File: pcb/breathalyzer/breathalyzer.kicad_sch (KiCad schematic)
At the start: 26 parts, among them IC1 TPS3840DL25DBVR, IC2 HEF4543BT,653, J1 Conn_01x07_Pin, SW1 PTS636SK43SMTR, SW2 430162085826, U1 STM32F030K6Tx, U2 TLV73325PDBV, U3 TLV61070ADBV, U4 HDSP-211C, U5 HDSP-211C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

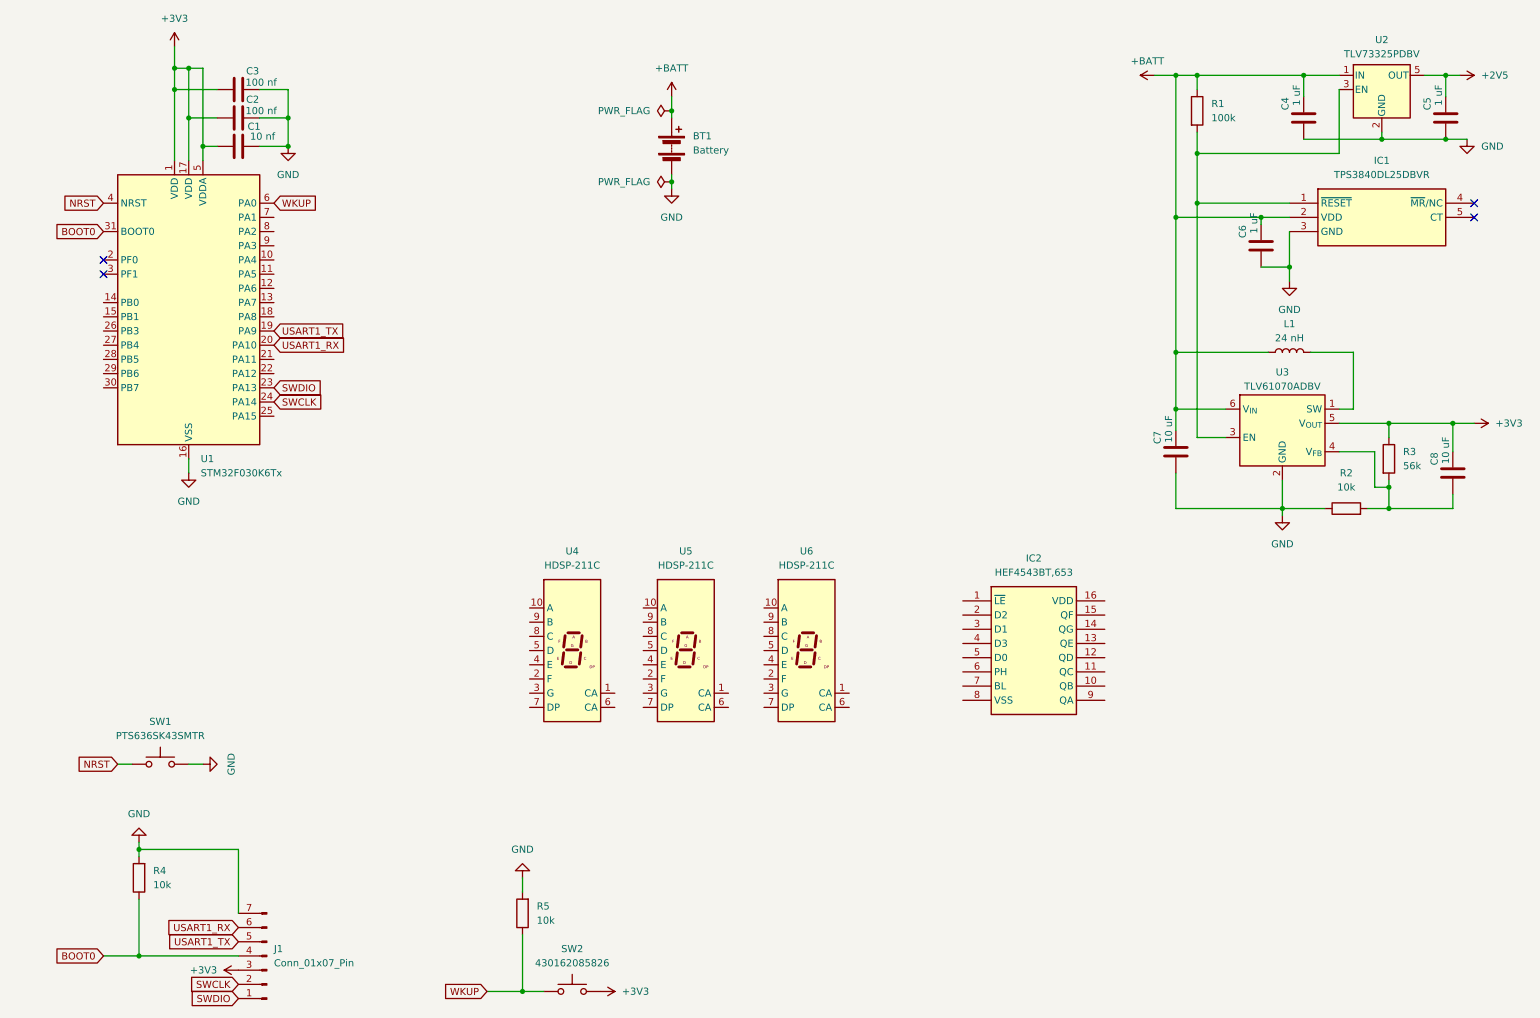
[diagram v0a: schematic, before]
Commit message: numeric LCD display and driver
+5V boost
previous parts scrapped
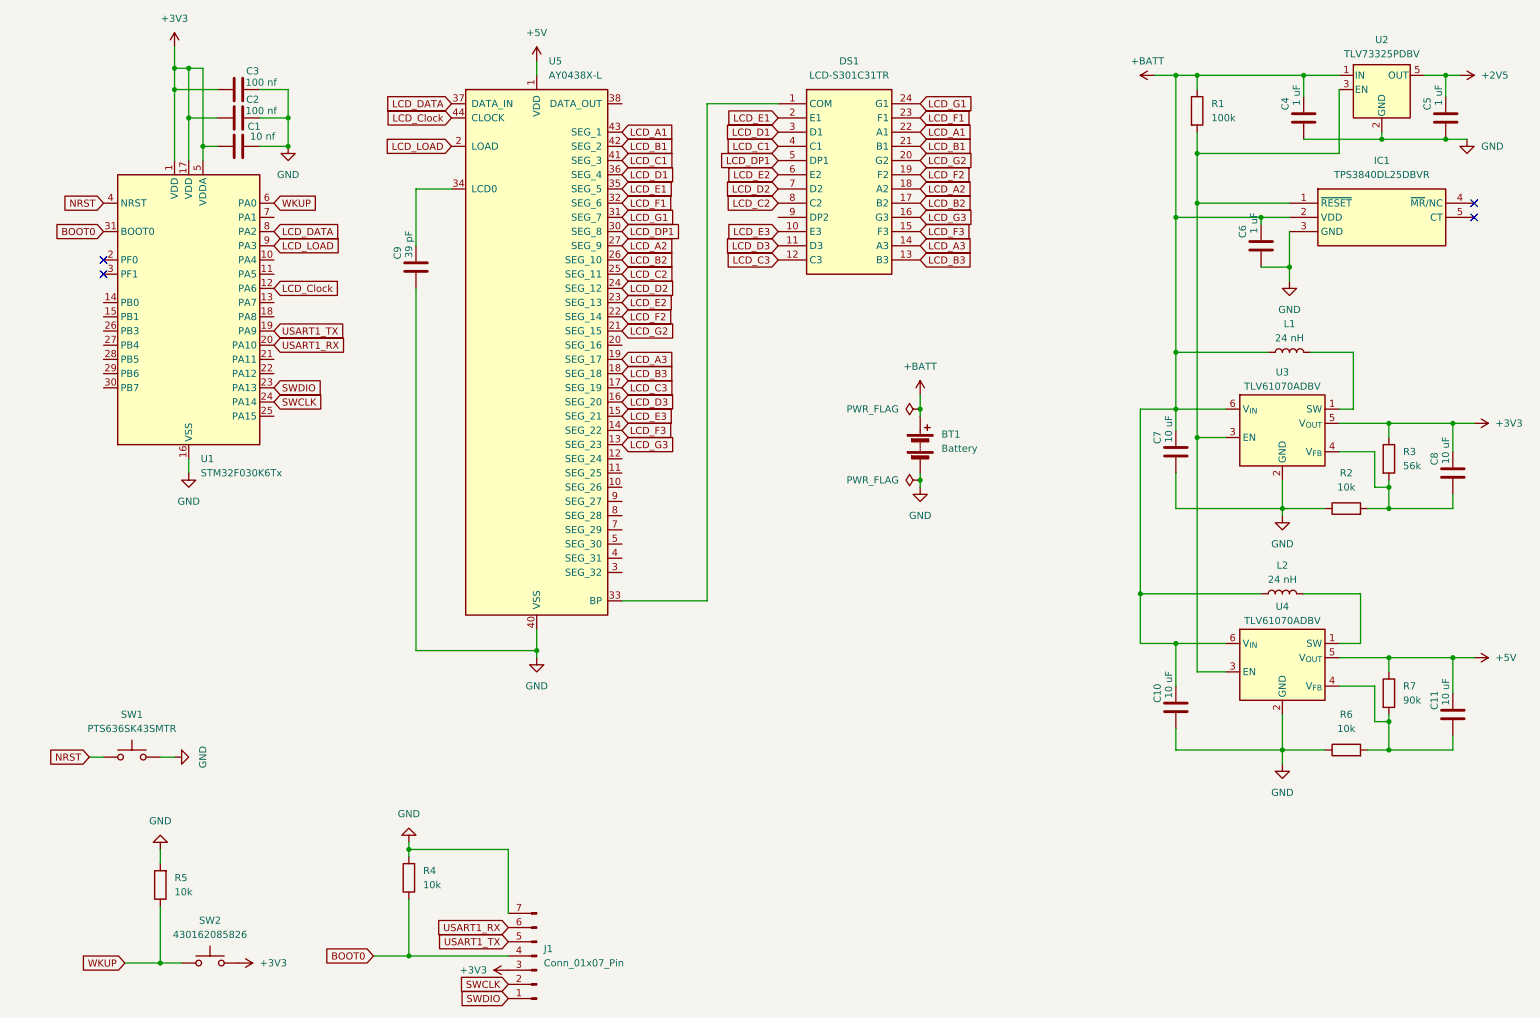
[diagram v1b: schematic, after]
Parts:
- removed IC2: HEF4543BT,653, breathalyzer:HEF4543BT653, symbol breathalyzer:HEF4543BT,653
- removed U4, U5, U6: HDSP-211C, breathalyzer:LDSA3502RDSUG, symbol Display_Character:HDSP-7401
- added C10, C11: 10 uF, Capacitor_SMD:C_0805_2012Metric, symbol Device:C
- added C9: 39 pF, Capacitor_SMD:C_0603_1608Metric, symbol Device:C
- added DS1: LCD-S301C31TR, LCD-S301C31TR, symbol breathalyzer:LCD-S301C31TR
- added L2: 24 nH, Inductor_SMD:L_1008_2520Metric, symbol Device:L
- added R6: 10k, Resistor_SMD:R_0603_1608Metric, symbol Device:R
- added R7: 90k, Resistor_SMD:R_1206_3216Metric, symbol Device:R
- added U4: TLV61070ADBV, Package_TO_SOT_SMD:SOT-23-6, symbol Regulator_Switching:TLV61070ADBV
- added U5: AY0438X-L, Package_LCC:PLCC-44, symbol Driver_Display:AY0438X-L
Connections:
- net +BATT: now also C10.2, L2.1, U4.6 (V_{IN})
- net GND: now also C10.1, C9.1, R6.1, U4.2 (GND), U5.40 (VSS)
- net at IC1.1 (~{RESET}), R1.2, U2.3 (EN)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: now also U4.3 (EN)
- net LCD_Clock: now reaches U1.12 (PA6)
- net LCD_Clock: now also U5.44 (CLOCK)
- net LCD_DATA: now reaches U1.8 (PA2)
- net LCD_DATA: now also U5.37 (DATA_IN)
- net LCD_LOAD: now reaches U1.9 (PA3)
- net LCD_LOAD: now also U5.2 (LOAD)
- new net: C11.1, R6.2, R7.2, U4.4 (V_{FB})
- new net: L2.2, U4.1 (SW)
- new net: C9.2, U5.34 (LCD0)
- new net: DS1.1 (COM), U5.33 (BP)
- new net +5V: C11.2, R7.1, U4.5 (V_{OUT}), U5.1 (VDD)
- new net LCD_A1: DS1.22 (A1), U5.43 (SEG_1)
- new net LCD_A2: DS1.18 (A2), U5.27 (SEG_9)
- new net LCD_A3: DS1.14 (A3), U5.19 (SEG_17)
- new net LCD_B1: DS1.21 (B1), U5.42 (SEG_2)
- new net LCD_B2: DS1.17 (B2), U5.26 (SEG_10)
- new net LCD_B3: DS1.13 (B3), U5.18 (SEG_18)
- new net LCD_C1: DS1.4 (C1), U5.41 (SEG_3)
- new net LCD_C2: DS1.8 (C2), U5.25 (SEG_11)
- new net LCD_C3: DS1.12 (C3), U5.17 (SEG_19)
- new net LCD_D1: DS1.3 (D1), U5.36 (SEG_4)
- new net LCD_D2: DS1.7 (D2), U5.24 (SEG_12)
- new net LCD_D3: DS1.11 (D3), U5.16 (SEG_20)
- new net LCD_DP1: DS1.5 (DP1), U5.30 (SEG_8)
- new net LCD_E1: DS1.2 (E1), U5.35 (SEG_5)
- new net LCD_E2: DS1.6 (E2), U5.23 (SEG_13)
- new net LCD_E3: DS1.10 (E3), U5.15 (SEG_21)
- new net LCD_F1: DS1.23 (F1), U5.32 (SEG_6)
- new net LCD_F2: DS1.19 (F2), U5.22 (SEG_14)
- new net LCD_F3: DS1.15 (F3), U5.14 (SEG_22)
- new net LCD_G1: DS1.24 (G1), U5.31 (SEG_7)
- new net LCD_G2: DS1.20 (G2), U5.21 (SEG_15)
- new net LCD_G3: DS1.16 (G3), U5.13 (SEG_23)
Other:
- moved on the sheet: BT1, J1, R4, R5, SW1, SW2

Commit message: removed 3V3 boost
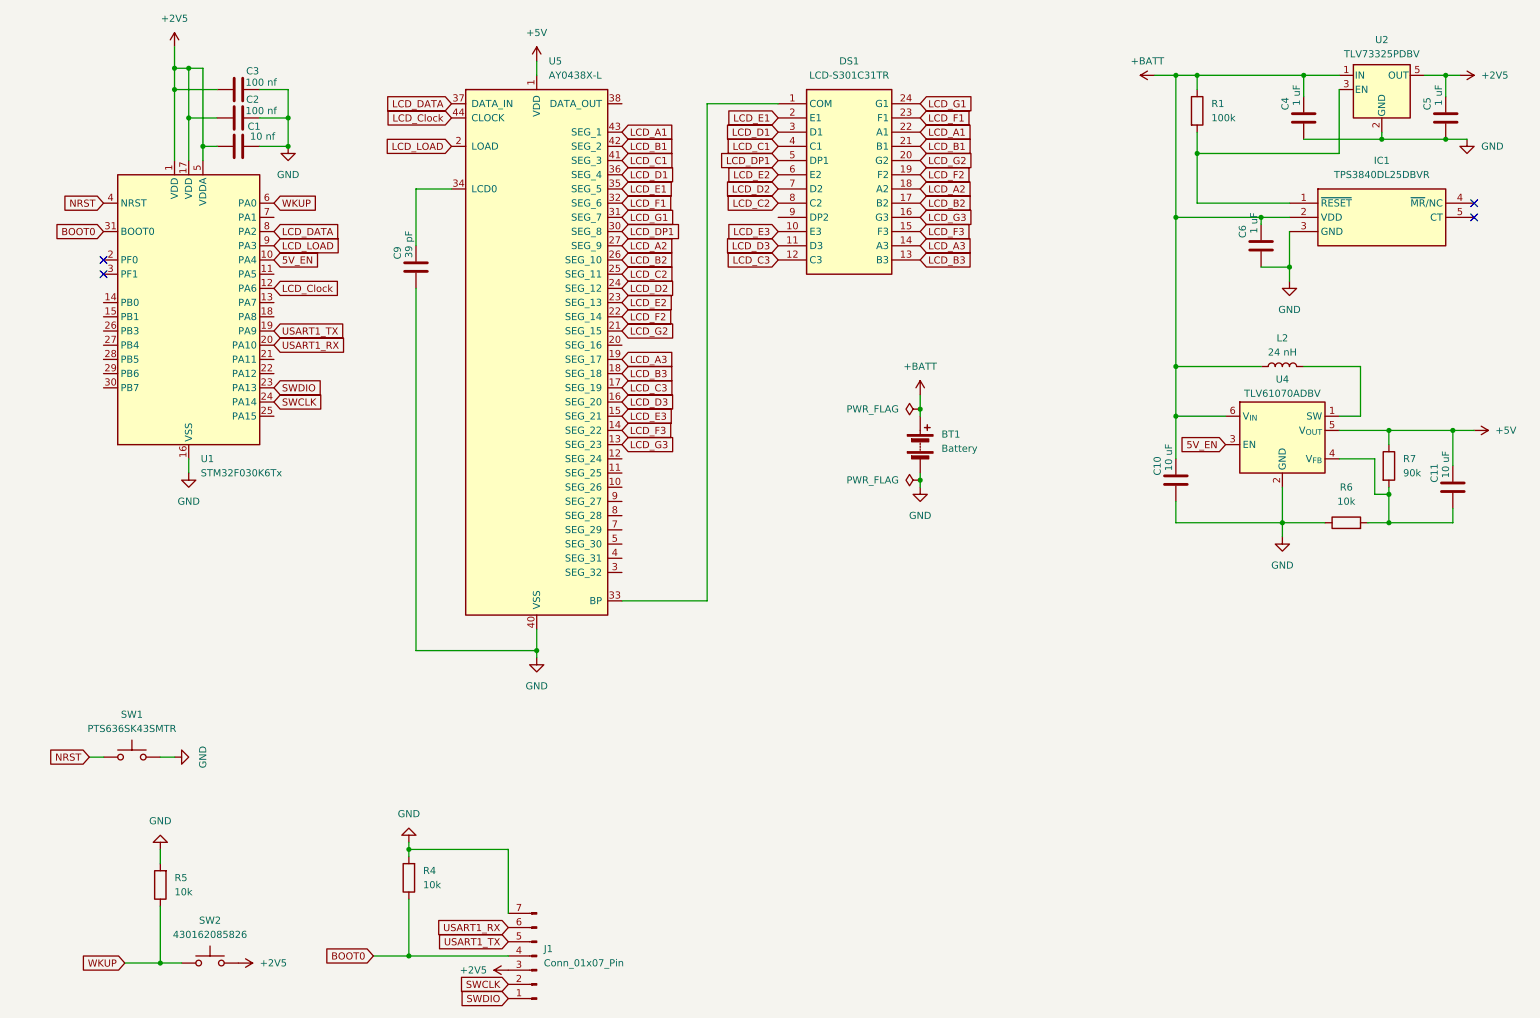
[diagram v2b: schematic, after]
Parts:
- removed C7, C8: 10 uF, Capacitor_SMD:C_0805_2012Metric, symbol Device:C
- removed L1: 24 nH, Inductor_SMD:L_1008_2520Metric, symbol Device:L
- removed R2: 10k, Resistor_SMD:R_0603_1608Metric, symbol Device:R
- removed R3: 56k, Resistor_SMD:R_0603_1608Metric, symbol Device:R
- removed U3: TLV61070ADBV, Package_TO_SOT_SMD:SOT-23-6, symbol Regulator_Switching:TLV61070ADBV
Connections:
- net +3V3 is gone; now on net +2V5: C1.1, C2.1, C3.1, J1.3 (Pin_3), SW2.2, U1.1 (VDD), U1.17 (VDD), U1.5 (VDDA)
- net at IC1.1 (~{RESET}), R1.2, U2.3 (EN): no longer U4.3 (EN)
- net 5V_EN: now reaches U1.10 (PA4)
- net 5V_EN: now also U4.3 (EN)
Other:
- moved on the sheet: C10, C11, L2, R6, R7, U4

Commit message: Userbutton
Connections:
- net WKUP is gone; now on net USERBUTTON: R5.1, SW2.1, U1.6 (PA0)
- net USERBUTTON: now reaches U1.15 (PB1)
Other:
- moved on the sheet: BT1
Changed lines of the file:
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@@
 	)
 	(junction
-		(at 175.26 83.82)
+		(at 262.89 132.08)
 		(diameter 0)
 		(color 0 0 0 0)
@@
 	)
 	(junction
-		(at 175.26 96.52)
+		(at 262.89 144.78)
 		(diameter 0)
 		(color 0 0 0 0)
@@
 	(wire
 		(pts
-			(xy 175.26 83.82) (xy 175.26 85.09)
+			(xy 262.89 132.08) (xy 262.89 133.35)
 		)
 		(stroke
@@
 	(wire
 		(pts
-			(xy 175.26 96.52) (xy 175.26 97.79)
+			(xy 262.89 144.78) (xy 262.89 146.05)
 		)
 		(stroke
@@
 	(wire
 		(pts
+			(xy 33.02 189.23) (xy 39.37 189.23)
+		)
+		(stroke
+			(width 0)
+			(type default)
+		)
+	)
+	(wire
+		(pts
+			(xy 39.37 189.23) (xy 39.37 182.88)
+		)
+		(stroke
+			(width 0)
+			(type default)
+		)
+	)
+	(wire
+		(pts
 			(xy 39.37 172.72) (xy 39.37 182.88)
 		)
@@
 	(wire
 		(pts
-			(xy 175.26 95.25) (xy 175.26 96.52)
+			(xy 262.89 143.51) (xy 262.89 144.78)
 		)
 		(stroke
@@
 	(wire
 		(pts
-			(xy 175.26 81.28) (xy 175.26 83.82)
+			(xy 262.89 129.54) (xy 262.89 132.08)
 		)
 		(stroke
@@
 		)
 	)
+	(global_label "USERBUTTON"
+		(shape input)
+		(at 33.02 189.23 180)
+		(fields_autoplaced yes)
+		(effects
+			(font
+				(size 1.27 1.27)
+			)
+			(justify right)
+		)
+		(property "Intersheetrefs" "${INTERSHEET_REFS}"
+			(at 17.8791 189.23 0)
+			(effects
+				(font
+					(size 1.27 1.27)
+				)
+				(justify right)
+				(hide yes)
+			)
+		)
+	)
 	(global_label "LCD_B3"
 		(shape input)
@@
 		)
 	)
+	(global_label "USERBUTTON"
+		(shape input)
+		(at 29.21 67.31 180)
+		(fields_autoplaced yes)
+		(effects
+			(font
+				(size 1.27 1.27)
+			)
+			(justify right)
+		)
+		(property "Intersheetrefs" "${INTERSHEET_REFS}"
+			(at 14.0691 67.31 0)
+			(effects
+				(font
+					(size 1.27 1.27)
+				)
+				(justify right)
+				(hide yes)
+			)
+		)
+	)
 	(global_label "LCD_C3"
 		(shape input)
@@
 	(symbol
 		(lib_id "power:GND")
-		(at 175.26 97.79 0)
+		(at 262.89 146.05 0)
 		(unit 1)
 		(exclude_from_sim no)
@@
 		(fields_autoplaced yes)
 		(property "Reference" "#PWR04"
-			(at 175.26 104.14 0)
+			(at 262.89 152.4 0)
 			(effects
 				(font
@@
 		)
 		(property "Value" "GND"
-			(at 175.26 102.87 0)
+			(at 262.89 151.13 0)
 			(effects
 				(font
@@
 		)
 		(property "Footprint" ""
-			(at 175.26 97.79 0)
+			(at 262.89 146.05 0)
 			(effects
 				(font
@@
 		)
 		(property "Datasheet" ""
-			(at 175.26 97.79 0)
+			(at 262.89 146.05 0)
 			(effects
 				(font
@@
 		)
 		(property "Description" "Power symbol creates a global label with name \"GND\" , ground"
-			(at 175.26 97.79 0)
+			(at 262.89 146.05 0)
 			(effects
 				(font
@@
 	(symbol
 		(lib_id "Device:Battery")
-		(at 175.26 90.17 0)
+		(at 262.89 138.43 0)
 		(unit 1)
 		(exclude_from_sim no)
@@
 		(fields_autoplaced yes)
 		(property "Reference" "BT1"
-			(at 179.07 88.3284 0)
+			(at 266.7 136.5884 0)
 			(effects
 				(font
@@
 		)
 		(property "Value" "Battery"
-			(at 179.07 90.8684 0)
+			(at 266.7 139.1284 0)
 			(effects
 				(font
@@
 		)
 		(property "Footprint" ""
-			(at 175.26 88.646 90)
+			(at 262.89 136.906 90)
 			(effects
 				(font
@@
 		)
 		(property "Datasheet" "~"
-			(at 175.26 88.646 90)
+			(at 262.89 136.906 90)
 			(effects
 				(font
@@
 		)
 		(property "Description" "Multiple-cell battery"
-			(at 175.26 90.17 0)
+			(at 262.89 138.43 0)
 			(effects
 				(font
@@
 	(symbol
 		(lib_id "power:PWR_FLAG")
-		(at 175.26 96.52 90)
+		(at 262.89 144.78 90)
 		(unit 1)
 		(exclude_from_sim no)
@@
 		(fields_autoplaced yes)
 		(property "Reference" "#FLG02"
-			(at 173.355 96.52 0)
+			(at 260.985 144.78 0)
 			(effects
 				(font
@@
 		)
 		(property "Value" "PWR_FLAG"
-			(at 171.45 96.5199 90)
+			(at 259.08 144.7799 90)
 			(effects
 				(font
@@
 		)
 		(property "Footprint" ""
-			(at 175.26 96.52 0)
+			(at 262.89 144.78 0)
 			(effects
 				(font
@@
 		)
 		(property "Datasheet" "~"
-			(at 175.26 96.52 0)
+			(at 262.89 144.78 0)
 			(effects
 				(font
@@
 		)
 		(property "Description" "Special symbol for telling ERC where power comes from"
-			(at 175.26 96.52 0)
+			(at 262.89 144.78 0)
 			(effects
 				(font
@@
 	(symbol
 		(lib_id "power:PWR_FLAG")
-		(at 175.26 83.82 90)
+		(at 262.89 132.08 90)
 		(unit 1)
 		(exclude_from_sim no)
@@
 		(fields_autoplaced yes)
 		(property "Reference" "#FLG01"
-			(at 173.355 83.82 0)
+			(at 260.985 132.08 0)
 			(effects
 				(font
@@
 		)
 		(property "Value" "PWR_FLAG"
-			(at 171.45 83.8199 90)
+			(at 259.08 132.0799 90)
 			(effects
 				(font
@@
 		)
 		(property "Footprint" ""
-			(at 175.26 83.82 0)
+			(at 262.89 132.08 0)
 			(effects
 				(font
@@
 		)
 		(property "Datasheet" "~"
-			(at 175.26 83.82 0)
+			(at 262.89 132.08 0)
 			(effects
 				(font
@@
 		)
 		(property "Description" "Special symbol for telling ERC where power comes from"
-			(at 175.26 83.82 0)
+			(at 262.89 132.08 0)
 			(effects
 				(font
@@
 	(symbol
 		(lib_id "power:+BATT")
-		(at 175.26 81.28 0)
+		(at 262.89 129.54 0)
 		(unit 1)
 		(exclude_from_sim no)
@@
 		(fields_autoplaced yes)
 		(property "Reference" "#PWR05"
-			(at 175.26 85.09 0)
+			(at 262.89 133.35 0)
 			(effects
 				(font
@@
 		)
 		(property "Value" "+BATT"
-			(at 175.26 76.2 0)
+			(at 262.89 124.46 0)
 			(effects
 				(font
@@
 		)
 		(property "Footprint" ""
-			(at 175.26 81.28 0)
+			(at 262.89 129.54 0)
 			(effects
 				(font
@@
 		)
 		(property "Datasheet" ""
-			(at 175.26 81.28 0)
+			(at 262.89 129.54 0)
 			(effects
 				(font
@@
 		)
 		(property "Description" "Power symbol creates a global label with name \"+BATT\""
-			(at 175.26 81.28 0)
+			(at 262.89 129.54 0)
 			(effects
 				(font

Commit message: buzzer
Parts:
- added BZ1: Buzzer, breathalyzer:CPT1414680T, symbol breathalyzer:Buzzer
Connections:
- net GND: now also BZ1.1 (+)
- net BUZZER: now reaches U1.18 (PA8)
- net BUZZER: now also BZ1.2 (-)
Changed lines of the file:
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@@
 	(wire
 		(pts
+			(xy 209.55 146.05) (xy 212.09 146.05)
+		)
+		(stroke
+			(width 0)
+			(type default)
+		)
+	)
+	(wire
+		(pts
 			(xy 224.79 38.1) (xy 224.79 46.99)
 		)
@@
 	(wire
 		(pts
+			(xy 209.55 143.51) (xy 209.55 146.05)
+		)
+		(stroke
+			(width 0)
+			(type default)
+		)
+	)
+	(wire
+		(pts
 			(xy 256.54 92.71) (xy 256.54 99.06)
 		)
@@
 	(wire
 		(pts
+			(xy 209.55 151.13) (xy 212.09 151.13)
+		)
+		(stroke
+			(width 0)
+			(type default)
+		)
+	)
+	(wire
+		(pts
 			(xy 44.45 22.86) (xy 44.45 31.75)
 		)
@@
 		)
 	)
+	(global_label "BUZZER"
+		(shape input)
+		(at 209.55 151.13 180)
+		(fields_autoplaced yes)
+		(effects
+			(font
+				(size 1.27 1.27)
+			)
+			(justify right)
+		)
+		(property "Intersheetrefs" "${INTERSHEET_REFS}"
+			(at 199.1263 151.13 0)
+			(effects
+				(font
+					(size 1.27 1.27)
+				)
+				(justify right)
+				(hide yes)
+			)
+		)
+	)
 	(global_label "LCD_B1"
 		(shape input)
@@
 		)
 	)
+	(global_label "BUZZER"
+		(shape input)
+		(at 59.69 67.31 0)
+		(fields_autoplaced yes)
+		(effects
+			(font
+				(size 1.27 1.27)
+			)
+			(justify left)
+		)
+		(property "Intersheetrefs" "${INTERSHEET_REFS}"
+			(at 70.1137 67.31 0)
+			(effects
+				(font
+					(size 1.27 1.27)
+				)
+				(justify left)
+				(hide yes)
+			)
+		)
+	)
 	(global_label "USERBUTTON"
 		(shape input)
@@
 	)
 	(symbol
+		(lib_id "breathalyzer:Buzzer")
+		(at 214.63 148.59 0)
+		(unit 1)
+		(exclude_from_sim no)
+		(in_bom yes)
+		(on_board yes)
+		(dnp no)
+		(fields_autoplaced yes)
+		(property "Reference" "BZ1"
+			(at 218.44 147.3199 0)
+			(effects
+				(font
+					(size 1.27 1.27)
+				)
+				(justify left)
+			)
+		)
+		(property "Value" "Buzzer"
+			(at 218.44 149.8599 0)
+			(effects
+				(font
+					(size 1.27 1.27)
+				)
+				(justify left)
+			)
+		)
+		(property "Footprint" "breathalyzer:CPT1414680T"
+			(at 213.995 146.05 90)
+			(effects
+				(font
+					(size 1.27 1.27)
+				)
+				(hide yes)
+			)
+		)
+		(property "Datasheet" "https://hu.mouser.com/ProductDetail/Same-Sky/CPT-14146-80T?qs=pBJMDPsKWf3pym5QY1xQDQ%3D%3D"
+			(at 213.995 146.05 90)
+			(effects
+				(font
+					(size 1.27 1.27)
+				)
+				(hide yes)
+			)
+		)
+		(property "Description" "Buzzer"
+			(at 214.63 148.59 0)
+			(effects
+				(font
+					(size 1.27 1.27)
+				)
+				(hide yes)
+			)
+		)
+		(pin "2"
+		)
+		(pin "1"
+		)
+		(instances
+			(project ""
+				(path "/e92d6a20-f7e6-42bc-b7eb-52ddd833ed75"
+					(reference "BZ1")
+					(unit 1)
+				)
+			)
+		)
+	)
+	(symbol
 		(lib_id "power:+2V5")
 		(at 271.78 24.13 270)
@@
 					(unit 1)
 				)
+			)
+		)
+	)
+	(symbol
+		(lib_id "power:GND")
+		(at 209.55 143.51 180)
+		(unit 1)
+		(exclude_from_sim no)
+		(in_bom yes)
+		(on_board yes)
+		(dnp no)
+		(fields_autoplaced yes)
+		(property "Reference" "#PWR014"
+			(at 209.55 137.16 0)
+			(effects
+				(font
+					(size 1.27 1.27)
+				)
+				(hide yes)
+			)
+		)
+		(property "Value" "GND"
+			(at 209.55 138.43 0)
+			(effects
+				(font
+					(size 1.27 1.27)
+				)
+			)
+		)
+		(property "Footprint" ""
+			(at 209.55 143.51 0)
+			(effects
+				(font
+					(size 1.27 1.27)
+				)
+				(hide yes)
+			)
+		)
+		(property "Datasheet" ""
+			(at 209.55 143.51 0)
+			(effects
+				(font
+					(size 1.27 1.27)
+				)
+				(hide yes)
+			)
+		)
+		(property "Description" "Power symbol creates a global label with name \"GND\" , ground"
+			(at 209.55 143.51 0)
+			(effects
+				(font
+					(size 1.27 1.27)
+				)
+				(hide yes)
+			)
+		)
+		(pin "1"
+		)
+		(instances
+			(project ""
+				(path "/e92d6a20-f7e6-42bc-b7eb-52ddd833ed75"
+					(reference "#PWR014")
+					(unit 1)
+				)
